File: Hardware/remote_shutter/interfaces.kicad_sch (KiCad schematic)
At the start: 12 parts, among them J2 OLED, J3 AudioJack3, Q1 DMN2056U, Q2 DMN2056U, SW1 RotaryEncoder_Switch

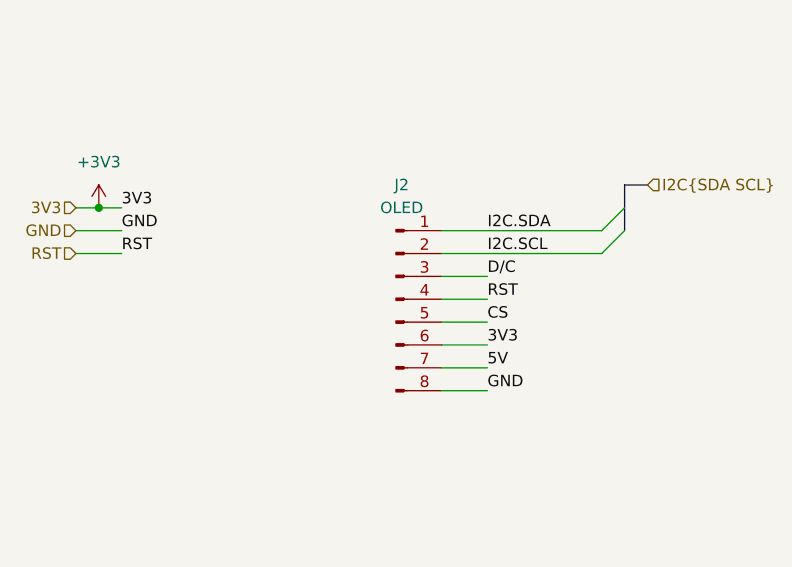
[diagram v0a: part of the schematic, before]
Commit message: Added debug connectors
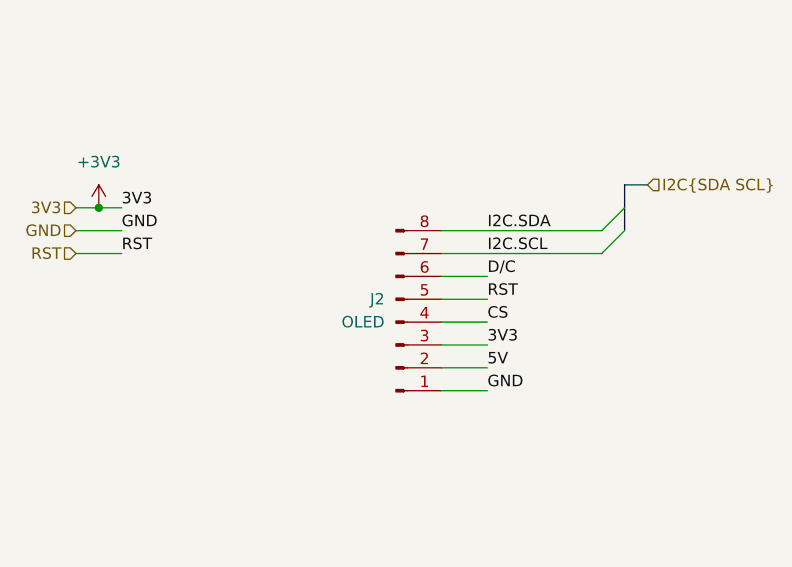
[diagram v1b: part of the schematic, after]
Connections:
- net +3V3: now also J2.3 (Pin_3); no longer J2.6 (Pin_6)
- net 5V: now also J2.2 (Pin_2); no longer J2.7 (Pin_7)
- net CS: now also J2.4 (Pin_4); no longer J2.5 (Pin_5)
- net D/C: now also J2.6 (Pin_6); no longer J2.3 (Pin_3)
- net GND: now also J2.1 (Pin_1); no longer J2.8 (Pin_8)
- net I2C.SCL: now also J2.7 (Pin_7); no longer J2.2 (Pin_2)
- net I2C.SDA: now also J2.8 (Pin_8); no longer J2.1 (Pin_1)
- net RST: now also J2.5 (Pin_5); no longer J2.4 (Pin_4)
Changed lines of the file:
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@@
+    (stroke (width 0) (type default) (color 0 0 0 0))
+  )
+  (wire (pts (xy 116.84 71.12) (xy 134.62 71.12))
+    (stroke (width 0) (type default) (color 0 0 0 0))
+  )
+  (wire (pts (xy 172.72 81.28) (xy 185.42 81.28))
+    (stroke (width 0) (type default) (color 0 0 0 0))
+  )
+  (bus (pts (xy 107.95 143.51) (xy 107.95 138.43))
+    (stroke (width 0) (type default) (color 0 0 0 0))
+  )
+  (wire (pts (xy 116.84 86.36) (xy 121.92 86.36))
+    (stroke (width 0) (type default) (color 0 0 0 0))
+  )
+  (wire (pts (xy 116.84 88.9) (xy 121.92 88.9))
+    (stroke (width 0) (type default) (color 0 0 0 0))
+  )
+  (wire (pts (xy 116.84 78.74) (xy 121.92 78.74))
+    (stroke (width 0) (type default) (color 0 0 0 0))
+  )
+  (wire (pts (xy 110.49 140.97) (xy 114.3 140.97))
+    (stroke (width 0) (type default) (color 0 0 0 0))
+  )
+  (bus (pts (xy 107.95 157.48) (xy 107.95 143.51))
+    (stroke (width 0) (type default) (color 0 0 0 0))
+  )
+  (bus (pts (xy 137.16 71.12) (xy 137.16 68.58))
+    (stroke (width 0) (type default) (color 0 0 0 0))
+  )
+  (bus (pts (xy 107.95 138.43) (xy 107.95 132.08))
+    (stroke (width 0) (type default) (color 0 0 0 0))
+  )
+  (wire (pts (xy 194.31 107.95) (xy 194.31 100.33))
+    (stroke (width 0) (type default) (color 0 0 0 0))
+  )
+  (bus (pts (xy 152.4 157.48) (xy 107.95 157.48))
+    (stroke (width 0) (type default) (color 0 0 0 0))
+  )
+  (wire (pts (xy 175.26 127) (xy 184.15 127))
+    (stroke (width 0) (type default) (color 0 0 0 0))
+  )
+  (wire (pts (xy 175.26 107.95) (xy 175.26 119.38))
+    (stroke (width 0) (type default) (color 0 0 0 0))
+  )
+  (wire (pts (xy 195.58 100.33) (xy 194.31 100.33))
+    (stroke (width 0) (type default) (color 0 0 0 0))
+  )
+  (wire (pts (xy 149.86 140.97) (xy 144.78 140.97))
+    (stroke (width 0) (type default) (color 0 0 0 0))
+  )
+  (wire (pts (xy 172.72 49.53) (xy 181.61 49.53))
+    (stroke (width 0) (type default) (color 0 0 0 0))
+  )
+  (wire (pts (xy 172.72 77.47) (xy 172.72 81.28))
+    (stroke (width 0) (type default) (color 0 0 0 0))
+  )
+  (wire (pts (xy 76.2 68.58) (xy 78.74 68.58))
+    (stroke (width 0) (type default) (color 0 0 0 0))
+  )
+  (wire (pts (xy 116.84 73.66) (xy 134.62 73.66))
+    (stroke (width 0) (type default) (color 0 0 0 0))
+  )
+  (bus (pts (xy 137.16 68.58) (xy 137.16 66.04))
     (stroke (width 0) (type default) (color 0 0 0 0))
   )
@@
     (stroke (width 0) (type default) (color 0 0 0 0))
   )
-  (wire (pts (xy 172.72 81.28) (xy 185.42 81.28))
-    (stroke (width 0) (type default) (color 0 0 0 0))
-  )
-  (bus (pts (xy 107.95 143.51) (xy 107.95 138.43))
-    (stroke (width 0) (type default) (color 0 0 0 0))
-  )
-  (wire (pts (xy 110.49 140.97) (xy 114.3 140.97))
-    (stroke (width 0) (type default) (color 0 0 0 0))
-  )
-  (bus (pts (xy 107.95 157.48) (xy 107.95 143.51))
-    (stroke (width 0) (type default) (color 0 0 0 0))
-  )
-  (bus (pts (xy 137.16 71.12) (xy 137.16 68.58))
-    (stroke (width 0) (type default) (color 0 0 0 0))
-  )
-  (bus (pts (xy 107.95 138.43) (xy 107.95 132.08))
-    (stroke (width 0) (type default) (color 0 0 0 0))
-  )
-  (wire (pts (xy 194.31 107.95) (xy 194.31 100.33))
-    (stroke (width 0) (type default) (color 0 0 0 0))
-  )
-  (bus (pts (xy 152.4 157.48) (xy 107.95 157.48))
-    (stroke (width 0) (type default) (color 0 0 0 0))
-  )
-  (wire (pts (xy 175.26 127) (xy 184.15 127))
-    (stroke (width 0) (type default) (color 0 0 0 0))
-  )
-  (wire (pts (xy 175.26 107.95) (xy 175.26 119.38))
-    (stroke (width 0) (type default) (color 0 0 0 0))
-  )
-  (wire (pts (xy 195.58 100.33) (xy 194.31 100.33))
-    (stroke (width 0) (type default) (color 0 0 0 0))
-  )
-  (wire (pts (xy 116.84 88.9) (xy 121.92 88.9))
-    (stroke (width 0) (type default) (color 0 0 0 0))
-  )
-  (wire (pts (xy 149.86 140.97) (xy 144.78 140.97))
-    (stroke (width 0) (type default) (color 0 0 0 0))
-  )
-  (wire (pts (xy 172.72 49.53) (xy 181.61 49.53))
-    (stroke (width 0) (type default) (color 0 0 0 0))
-  )
-  (wire (pts (xy 172.72 77.47) (xy 172.72 81.28))
-    (stroke (width 0) (type default) (color 0 0 0 0))
-  )
-  (wire (pts (xy 76.2 68.58) (xy 78.74 68.58))
-    (stroke (width 0) (type default) (color 0 0 0 0))
-  )
-  (bus (pts (xy 137.16 68.58) (xy 137.16 66.04))
-    (stroke (width 0) (type default) (color 0 0 0 0))
-  )
   (wire (pts (xy 172.72 46.99) (xy 181.61 46.99))
     (stroke (width 0) (type default) (color 0 0 0 0))
@@
     (stroke (width 0) (type default) (color 0 0 0 0))
   )
-  (wire (pts (xy 116.84 71.12) (xy 134.62 71.12))
-    (stroke (width 0) (type default) (color 0 0 0 0))
-  )
   (wire (pts (xy 76.2 71.12) (xy 81.28 71.12))
     (stroke (width 0) (type default) (color 0 0 0 0))
@@
     (stroke (width 0) (type default) (color 0 0 0 0))
   )
-  (wire (pts (xy 116.84 86.36) (xy 121.92 86.36))
-    (stroke (width 0) (type default) (color 0 0 0 0))
-  )
   (wire (pts (xy 194.31 127) (xy 194.31 119.38))
     (stroke (width 0) (type default) (color 0 0 0 0))
@@
     (stroke (width 0) (type default) (color 0 0 0 0))
   )
-  (wire (pts (xy 116.84 73.66) (xy 134.62 73.66))
-    (stroke (width 0) (type default) (color 0 0 0 0))
-  )
   (wire (pts (xy 189.23 127) (xy 194.31 127))
     (stroke (width 0) (type default) (color 0 0 0 0))
@@
     (stroke (width 0) (type default) (color 0 0 0 0))
   )
-  (wire (pts (xy 116.84 78.74) (xy 121.92 78.74))
+  (wire (pts (xy 116.84 81.28) (xy 121.92 81.28))
     (stroke (width 0) (type default) (color 0 0 0 0))
   )
@@
   )
   (wire (pts (xy 129.54 146.05) (xy 114.3 146.05))
-    (stroke (width 0) (type default) (color 0 0 0 0))
-  )
-  (wire (pts (xy 116.84 81.28) (xy 121.92 81.28))
     (stroke (width 0) (type default) (color 0 0 0 0))
   )
@@
     (pin "2")
   )
-  (symbol (lib_id "Connector:Conn_01x08_Male") (at 111.76 78.74 0) (unit 1)
-    (in_bom yes) (on_board yes) (fields_autoplaced)
-    (property "Reference" "J2" (id 0) (at 112.395 66.04 0))
-    (property "Value" "OLED" (id 1) (at 112.395 68.58 0))
-    (property "Footprint" "Connector_PinSocket_2.54mm:PinSocket_1x08_P2.54mm_Vertical" (id 2) (at 111.76 78.74 0)
-      (effects (font (size 1.27 1.27)) hide)
-    )
-    (property "Datasheet" "~" (id 3) (at 111.76 78.74 0)
-      (effects (font (size 1.27 1.27)) hide)
-    )
+  (symbol (lib_id "Connector:Conn_01x08_Male") (at 111.76 81.28 0) (mirror x) (unit 1)
+    (in_bom yes) (on_board yes) (fields_autoplaced)
+    (property "Reference" "J2" (id 0) (at 110.49 78.7399 0)
+      (effects (font (size 1.27 1.27)) (justify right))
+    )
+    (property "Value" "OLED" (id 1) (at 110.49 81.2799 0)
+      (effects (font (size 1.27 1.27)) (justify right))
+    )
+    (property "Footprint" "Connector_PinSocket_2.54mm:PinSocket_1x08_P2.54mm_Vertical" (id 2) (at 111.76 81.28 0)
+      (effects (font (size 1.27 1.27)) hide)
+    )
+    (property "Datasheet" "~" (id 3) (at 111.76 81.28 0)
+      (effects (font (size 1.27 1.27)) hide)
+    )
